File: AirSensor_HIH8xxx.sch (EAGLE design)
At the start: 2 parts, among them U3 HIH8120-021-001

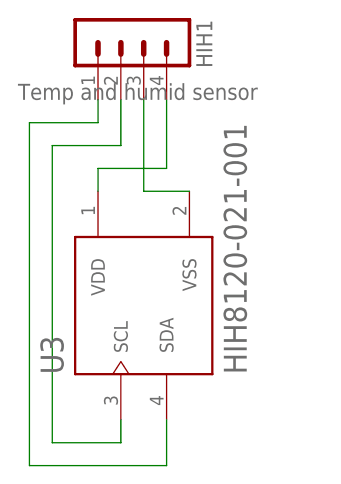
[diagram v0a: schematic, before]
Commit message: added JTAG schematic and PCB  + all pictures
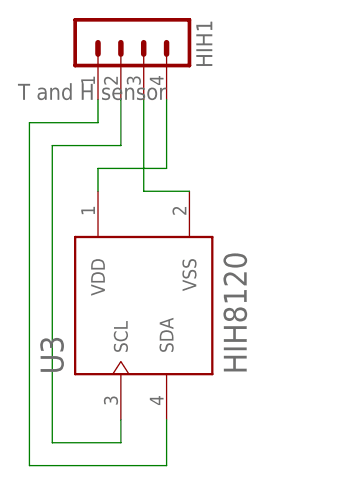
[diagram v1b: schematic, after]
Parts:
- HIH1: value Temp and humid sensor -> T and H sensor
- U3: value HIH8120-021-001 -> HIH8120
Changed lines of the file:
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@@
 </classes>
 <parts>
-<part name="HIH1" library="con-lstb" library_urn="urn:adsk.eagle:library:162" deviceset="MA04-1" device="" package3d_urn="urn:adsk.eagle:package:8337/1" value="Temp and humid sensor"/>
-<part name="U3" library="HIH8120-021-001" deviceset="HIH8120-021-001" device=""/>
+<part name="HIH1" library="con-lstb" library_urn="urn:adsk.eagle:library:162" deviceset="MA04-1" device="" package3d_urn="urn:adsk.eagle:package:8337/1" value="T and H sensor"/>
+<part name="U3" library="HIH8120-021-001" deviceset="HIH8120-021-001" device="" value="HIH8120"/>
 </parts>
 <sheets>
